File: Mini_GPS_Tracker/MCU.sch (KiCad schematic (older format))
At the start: 12 parts, among them SW3 Boot mode, U11 STM32F413ZHTx, Y1 32.786 KHz, Y3 8MHz

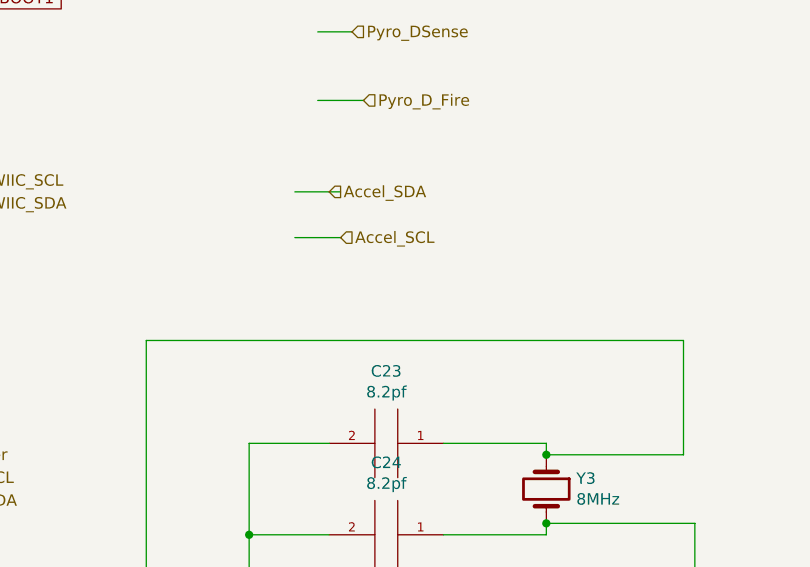
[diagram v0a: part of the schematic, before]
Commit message: Add files via upload
Adding 100 pin MCU
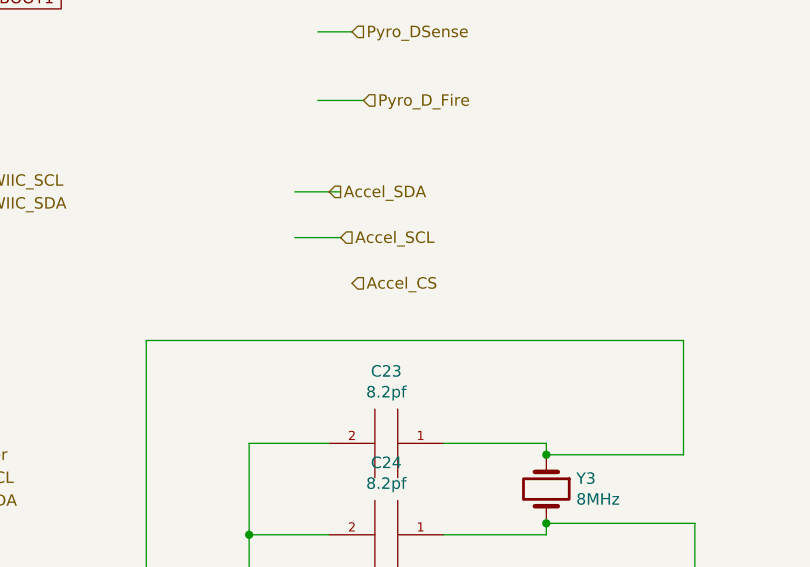
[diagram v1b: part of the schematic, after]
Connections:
- net labels added: Accel_CS

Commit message: Add files via upload
Making update for 100 pin CPU
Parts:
- R9: renamed from 10K1; value R -> 10K
- SW3: value Boot mode -> Boot Mode
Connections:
- net labels added: SWO, USB_RX, USB_TX
- net labels removed: A1, Accel_CS, PDMClock, PDMData, Pyro_A_Fire, Pyro_A_Sense, Pyro_B_Fire, Pyro_B_Sense, Pyro_C_Fire, Pyro_C_Sense, Pyro_DSense, Pyro_D_Fire, USB_RXI, USB_TX0
- wire segments 140 -> 129
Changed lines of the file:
@@
 EESchema Schematic File Version 4
+LIBS:Mini_GPS_Tracker-cache
 EELAYER 30 0
 EELAYER END
 $Descr A4 11693 8268
 encoding utf-8
-Sheet 9 11
+Sheet 7 9
 Title ""
 Date ""
@@
 Text HLabel 3600 6350 0    50   Input ~ 0
 GPS_RX
-Connection ~ 6200 3750
 Connection ~ 6200 1050
-Text HLabel 8150 4100 2    50   Input ~ 0
-Accel_CS
-Wire Wire Line
-	7900 3900 8100 3900
-Wire Wire Line
-	7900 3700 8100 3700
-Text HLabel 8100 3900 2    50   Input ~ 0
+Wire Wire Line
+	6200 4050 6400 4050
+Wire Wire Line
+	6200 4150 6400 4150
+Text HLabel 6400 4050 2    50   Input ~ 0
 Accel_SCL
-Text HLabel 8050 3700 2    50   Input ~ 0
+Text HLabel 6350 4150 2    50   Input ~ 0
 Accel_SDA
 Wire Wire Line
@@
 	0    1    1    0
 $EndComp
-Wire Wire Line
-	8150 3000 8000 3000
-Wire Wire Line
-	8200 3300 8000 3300
-Text HLabel 8150 3000 2    50   Input ~ 0
-Pyro_DSense
-Text HLabel 8200 3300 2    50   Input ~ 0
-Pyro_D_Fire
-Wire Wire Line
-	8150 2400 8000 2400
-Wire Wire Line
-	8200 2700 8000 2700
-Text HLabel 8150 2400 2    50   Input ~ 0
-Pyro_C_Sense
-Text HLabel 8200 2700 2    50   Input ~ 0
-Pyro_C_Fire
-Wire Wire Line
-	8150 1850 8000 1850
-Wire Wire Line
-	8200 2150 8000 2150
-Text HLabel 8150 1850 2    50   Input ~ 0
-Pyro_B_Sense
-Text HLabel 8200 2150 2    50   Input ~ 0
-Pyro_B_Fire
-Wire Wire Line
-	8200 1200 8050 1200
-Wire Wire Line
-	8250 1500 8050 1500
-Text HLabel 8200 1200 2    50   Input ~ 0
-Pyro_A_Sense
-Text HLabel 8250 1500 2    50   Input ~ 0
-Pyro_A_Fire
-Text HLabel 6700 6650 2    50   Input ~ 0
-PDMData
-Text HLabel 6700 6250 2    50   Input ~ 0
-PDMClock
-Text HLabel 6400 5050 2    50   Input ~ 0
+Text HLabel 6400 3450 2    50   Input ~ 0
 9_SDA
-Text HLabel 6400 4950 2    50   Input ~ 0
+Text HLabel 6400 1750 2    50   Input ~ 0
 9_SCL
 Text HLabel 6350 4850 2    50   Input ~ 0
 buzzer
-Text HLabel 6450 3750 2    50   Input ~ 0
+Text HLabel 6400 3350 2    50   Input ~ 0
 QWIIC_SDA
-Text HLabel 6450 3650 2    50   Input ~ 0
+Text HLabel 6450 3250 2    50   Input ~ 0
 QWIIC_SCL
 Text HLabel 6350 2950 2    50   Input ~ 0
-A1
+SWO
 Text HLabel 6350 2750 2    50   Input ~ 0
 cs_flash
@@
 SWDIO
 Text HLabel 6350 2050 2    50   Input ~ 0
-USB_RXI
-Text HLabel 6350 1950 2    50   Input ~ 0
-USB_TX0
+USB_RX
+Text HLabel 6350 2150 2    50   Input ~ 0
+USB_TX
 Text HLabel 6400 1650 2    50   Input ~ 0
 MOSI_Flash
 Text HLabel 6350 1550 2    50   Input ~ 0
 MISO_Flash
-Wire Wire Line
-	6200 6650 6700 6650
-Wire Wire Line
-	6200 6250 6700 6250
 Text HLabel 6400 1450 2    50   Input ~ 0
 clk_flash
@@
 TRANS_RX
 Wire Wire Line
-	6200 4950 6400 4950
-Wire Wire Line
-	6200 5050 6400 5050
+	6200 1750 6400 1750
+Wire Wire Line
+	6200 3450 6400 3450
 Wire Wire Line
 	6200 2250 6400 2250
@@
 	6200 1350 6350 1350
 Wire Wire Line
-	6200 1950 6350 1950
+	6200 2150 6350 2150
 Wire Wire Line
 	6200 2050 6350 2050
@@
 	6200 1450 6400 1450
 Wire Wire Line
-	6200 3650 6450 3650
-Wire Wire Line
-	6200 3750 6450 3750
+	6200 3250 6450 3250
+Wire Wire Line
+	6150 3350 6200 3350
 Wire Wire Line
 	6200 1050 6350 1050
-$Comp
-L Switch:SW_DIP_x02 SW3
-U 1 1 5EA164ED
-P 10400 1650
-F 0 "SW3" H 10400 2017 50  0000 C CNN
-F 1 "Boot mode" H 10400 1926 50  0000 C CNN
-F 2 "" H 10400 1650 50  0001 C CNN
-F 3 "~" H 10400 1650 50  0001 C CNN
-	1    10400 1650
-	1    0    0    -1
-$EndComp
-Connection ~ 10700 1650
-Wire Wire Line
-	10700 1550 10700 1650
-Wire Wire Line
-	10700 1900 10700 1650
 $Comp
 L power:GND #PWR036
@@
 Text GLabel 9850 1550 0    50   Input ~ 0
 BOOT0
-Text GLabel 9850 1650 0    50   Input ~ 0
-BOOT1
 Wire Wire Line
 	9850 1550 10000 1550
 Connection ~ 10000 1550
-Wire Wire Line
-	9850 1650 10000 1650
-Connection ~ 10000 1650
-$Comp
-L Device:R 10K1
+$Comp
+L Device:R R9
 U 1 1 5EA164D8
 P 10000 1350
-F 0 "10K1" H 10070 1396 50  0000 L CNN
-F 1 "R" H 10070 1305 50  0000 L CNN
+F 0 "R9" H 10070 1396 50  0000 L CNN
+F 1 "10K" H 10070 1305 50  0000 L CNN
 F 2 "" V 9930 1350 50  0001 C CNN
 F 3 "~" H 10000 1350 50  0001 C CNN
@@
 	1    0    0    -1
 $EndComp
-$Comp
-L Device:R R10
-U 1 1 5EA164D2
-P 10000 1800
-F 0 "R10" H 10070 1846 50  0000 L CNN
-F 1 "10K" H 10070 1755 50  0000 L CNN
-F 2 "" V 9930 1800 50  0001 C CNN
-F 3 "~" H 10000 1800 50  0001 C CNN
-	1    10000 1800
-	1    0    0    -1
-$EndComp
-Wire Wire Line
-	10000 1650 10100 1650
 $Comp
 L power:+3.3V #PWR034
@@
 	1    0    0    -1
 $EndComp
-$Comp
-L power:+3.3V #PWR035
-U 1 1 5EA164C5
-P 10100 2250
-F 0 "#PWR035" H 10100 2100 50  0001 C CNN
-F 1 "+3.3V" H 10115 2423 50  0000 C CNN
-F 2 "" H 10100 2250 50  0001 C CNN
-F 3 "" H 10100 2250 50  0001 C CNN
-	1    10100 2250
-	1    0    0    -1
-$EndComp
 Wire Wire Line
 	10000 1500 10000 1550
@@
 Wire Wire Line
 	10000 1200 10000 1100
-Wire Wire Line
-	10000 1950 10000 2250
-Wire Wire Line
-	10000 2250 10100 2250
 Text GLabel 6550 2850 2    50   Input ~ 0
 BOOT1
 Wire Wire Line
 	6200 2850 6550 2850
+Wire Wire Line
+	10700 1550 10700 1650
+Connection ~ 6200 3350
+Wire Wire Line
+	6200 3350 6400 3350
+$Comp
+L Switch:SW_DIP_x02 SW3
+U 1 1 5EABB9AD
+P 10400 1650
+F 0 "SW3" H 10400 2017 50  0000 C CNN
+F 1 "Boot Mode" H 10400 1926 50  0000 C CNN
+F 2 "" H 10400 1650 50  0001 C CNN
+F 3 "~" H 10400 1650 50  0001 C CNN
+	1    10400 1650
+	1    0    0    -1
+$EndComp
+Wire Wire Line
+	10700 1650 10700 1900
+Connection ~ 10700 1650
+Text GLabel 9850 1650 0    50   Input ~ 0
+BOOT1
+Wire Wire Line
+	9850 1650 10000 1650
+$Comp
+L Device:R R10
+U 1 1 5EAC9335
+P 10000 1800
+F 0 "R10" H 10070 1846 50  0000 L CNN
+F 1 "10K" H 10070 1755 50  0000 L CNN
+F 2 "" V 9930 1800 50  0001 C CNN
+F 3 "~" H 10000 1800 50  0001 C CNN
+	1    10000 1800
+	1    0    0    -1
+$EndComp
+Connection ~ 10000 1650
+Wire Wire Line
+	10000 1650 10100 1650
+$Comp
+L power:+3.3V #PWR05
+U 1 1 5EAC9AFE
+P 10000 2050
+F 0 "#PWR05" H 10000 1900 50  0001 C CNN
+F 1 "+3.3V" H 10015 2223 50  0000 C CNN
+F 2 "" H 10000 2050 50  0001 C CNN
+F 3 "" H 10000 2050 50  0001 C CNN
+	1    10000 2050
+	-1   0    0    1
+$EndComp
 $EndSCHEMATC
